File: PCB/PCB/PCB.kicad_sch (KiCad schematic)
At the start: 28 parts, among them J2 USB_B_Micro, Q1 BC817, Q2 BC817, Q3 BSS84, U1 ESP32-S3-WROOM-1, U2 CP2102N-Axx-xQFN28, U3 NCP1117-3.3_SOT223, U4 UDA1334ATS, U5 PAM8403D

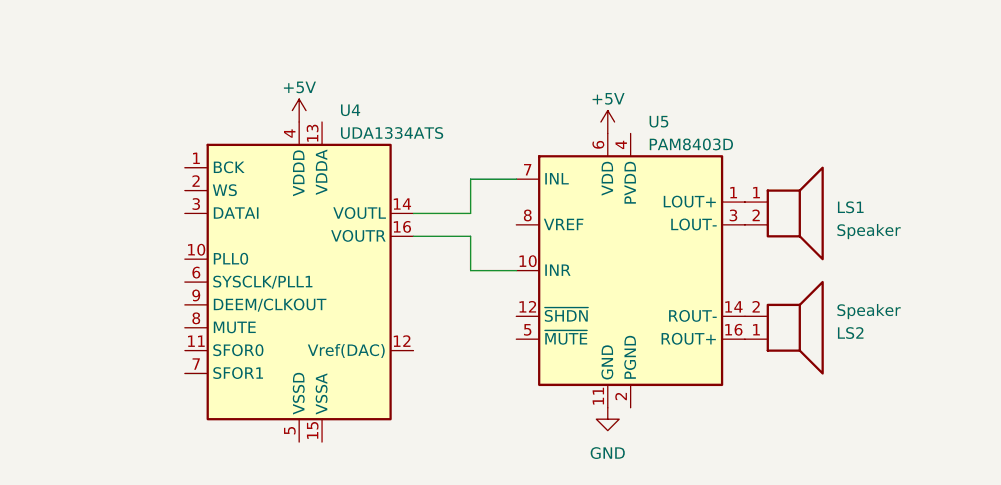
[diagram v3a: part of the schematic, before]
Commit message: added Audio Processing
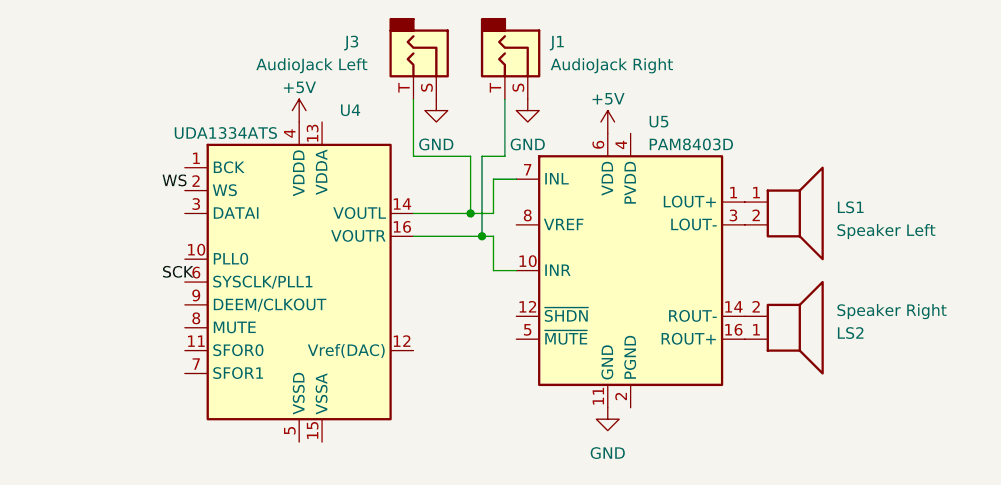
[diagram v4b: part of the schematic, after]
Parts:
- added J1: AudioJack Right, Connector_Audio:Jack_XLR_Neutrik_NC3FAAH1-0_Horizontal, symbol Connector_Audio:AudioJack2
- added J3: AudioJack Left, symbol Connector_Audio:AudioJack2
- LS1: value Speaker -> Speaker Left
- LS2: value Speaker -> Speaker Right
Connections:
- net GND: now also J1.S, J3.S
- net at U4.16 (VOUTR), U5.10 (INR): now also J1.T
- net at U4.14 (VOUTL), U5.7 (INL): now also J3.T
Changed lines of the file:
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@@
   (junction (at 41.91 93.98) (diameter 0) (color 0 0 0 0)
   )
+  (junction (at 314.96 36.83) (diameter 0) (color 0 0 0 0)
+  )
   (junction (at 50.8 81.28) (diameter 0) (color 0 0 0 0)
   )
@@
   )
   (junction (at 24.13 104.14) (diameter 0) (color 0 0 0 0)
+  )
+  (junction (at 313.69 34.29) (diameter 0) (color 0 0 0 0)
   )
   (junction (at 71.12 71.12) (diameter 0) (color 0 0 0 0)
@@
     (stroke (width 0) (type default))
   )
+  (wire (pts (xy 313.69 27.94) (xy 313.69 34.29))
+    (stroke (width 0) (type default))
+  )
+  (wire (pts (xy 314.96 36.83) (xy 316.23 36.83))
+    (stroke (width 0) (type default))
+  )
+  (wire (pts (xy 313.69 34.29) (xy 316.23 34.29))
+    (stroke (width 0) (type default))
+  )
   (wire (pts (xy 57.15 76.2) (xy 58.42 76.2))
     (stroke (width 0) (type default))
@@
     (stroke (width 0) (type default))
   )
-  (wire (pts (xy 313.69 34.29) (xy 313.69 30.48))
+  (wire (pts (xy 316.23 34.29) (xy 316.23 30.48))
     (stroke (width 0) (type default))
   )
@@
     (stroke (width 0) (type default))
   )
-  (wire (pts (xy 307.34 36.83) (xy 313.69 36.83))
+  (wire (pts (xy 307.34 36.83) (xy 314.96 36.83))
     (stroke (width 0) (type default))
   )
@@
     (stroke (width 0) (type default))
   )
-  (wire (pts (xy 313.69 30.48) (xy 318.77 30.48))
+  (wire (pts (xy 316.23 30.48) (xy 318.77 30.48))
     (stroke (width 0) (type default))
   )
@@
     (stroke (width 0) (type default))
   )
+  (wire (pts (xy 307.34 21.59) (xy 307.34 27.94))
+    (stroke (width 0) (type default))
+  )
   (wire (pts (xy 41.91 93.98) (xy 41.91 104.14))
     (stroke (width 0) (type default))
@@
     (stroke (width 0) (type default))
   )
-  (wire (pts (xy 313.69 36.83) (xy 313.69 40.64))
+  (wire (pts (xy 316.23 36.83) (xy 316.23 40.64))
     (stroke (width 0) (type default))
   )
@@
     (stroke (width 0) (type default))
   )
+  (wire (pts (xy 317.5 27.94) (xy 314.96 27.94))
+    (stroke (width 0) (type default))
+  )
   (wire (pts (xy 46.99 88.9) (xy 46.99 109.22))
     (stroke (width 0) (type default))
@@
     (stroke (width 0) (type default))
   )
+  (wire (pts (xy 314.96 27.94) (xy 314.96 36.83))
+    (stroke (width 0) (type default))
+  )
   (wire (pts (xy 116.84 60.96) (xy 144.78 60.96))
     (stroke (width 0) (type default))
@@
     (stroke (width 0) (type default))
   )
-  (wire (pts (xy 313.69 40.64) (xy 318.77 40.64))
+  (wire (pts (xy 316.23 40.64) (xy 318.77 40.64))
     (stroke (width 0) (type default))
   )
@@
     (stroke (width 0) (type default))
   )
+  (wire (pts (xy 307.34 27.94) (xy 313.69 27.94))
+    (stroke (width 0) (type default))
+  )
   (wire (pts (xy 111.76 78.74) (xy 111.76 46.99))
     (stroke (width 0) (type default))
@@
   )
   (wire (pts (xy 86.36 97.79) (xy 86.36 88.9))
+    (stroke (width 0) (type default))
+  )
+  (wire (pts (xy 317.5 21.59) (xy 317.5 27.94))
     (stroke (width 0) (type default))
   )
@@
     (effects (font (size 1.27 1.27)) (justify left bottom))
   )
+  (label "WS" (at 279.4 31.75 0) (fields_autoplaced)
+    (effects (font (size 1.27 1.27)) (justify left bottom))
+  )
   (label "txd" (at 83.82 76.2 0) (fields_autoplaced)
     (effects (font (size 1.27 1.27)) (justify left bottom))
@@
   )
   (label "EN" (at 113.03 83.82 0) (fields_autoplaced)
+    (effects (font (size 1.27 1.27)) (justify left bottom))
+  )
+  (label "SCK" (at 279.4 41.91 0) (fields_autoplaced)
     (effects (font (size 1.27 1.27)) (justify left bottom))
   )
@@
     )
   )
+  (symbol (lib_id "power:GND") (at 320.04 21.59 0) (unit 1)
+    (in_bom yes) (on_board yes) (dnp no) (fields_autoplaced)
+    (property "Reference" "#PWR021" (at 320.04 27.94 0)
+      (effects (font (size 1.27 1.27)) hide)
+    )
+    (property "Value" "GND" (at 320.04 26.67 0)
+      (effects (font (size 1.27 1.27)))
+    )
+    (property "Footprint" "" (at 320.04 21.59 0)
+      (effects (font (size 1.27 1.27)) hide)
+    )
+    (property "Datasheet" "" (at 320.04 21.59 0)
+      (effects (font (size 1.27 1.27)) hide)
+    )
+    (pin "1")
+    (instances
+      (project "PCB"
+        (path "/8a45fe01-405d-4f4d-910d-01ae941f9b06"
+          (reference "#PWR021") (unit 1)
+        )
+      )
+    )
+  )
   (symbol (lib_id "power:GND") (at 59.69 36.83 0) (unit 1)
     (in_bom yes) (on_board yes) (dnp no) (fields_autoplaced)
@@
       (effects (font (size 1.27 1.27)) (justify left))
     )
-    (property "Value" "Speaker" (at 354.33 36.195 0)
+    (property "Value" "Speaker Left" (at 354.33 36.195 0)
       (effects (font (size 1.27 1.27)) (justify left))
     )
@@
       (effects (font (size 1.27 1.27)) (justify left))
     )
-    (property "Value" "Speaker" (at 354.33 45.085 0)
+    (property "Value" "Speaker Right" (at 354.33 45.085 0)
       (effects (font (size 1.27 1.27)) (justify left))
     )
@@
   )
   (symbol (lib_id "Audio:UDA1334ATS") (at 294.64 41.91 0) (unit 1)
-    (in_bom yes) (on_board yes) (dnp no) (fields_autoplaced)
+    (in_bom yes) (on_board yes) (dnp no)
     (property "Reference" "U4" (at 299.1359 22.86 0)
       (effects (font (size 1.27 1.27)) (justify left))
     )
-    (property "Value" "UDA1334ATS" (at 299.1359 25.4 0)
+    (property "Value" "UDA1334ATS" (at 280.67 25.4 0)
       (effects (font (size 1.27 1.27)) (justify left))
     )
@@
         (path "/8a45fe01-405d-4f4d-910d-01ae941f9b06"
           (reference "R7") (unit 1)
+        )
+      )
+    )
+  )
+  (symbol (lib_id "power:GND") (at 309.88 21.59 0) (unit 1)
+    (in_bom yes) (on_board yes) (dnp no)
+    (property "Reference" "#PWR022" (at 309.88 27.94 0)
+      (effects (font (size 1.27 1.27)) hide)
+    )
+    (property "Value" "GND" (at 309.88 26.67 0)
+      (effects (font (size 1.27 1.27)))
+    )
+    (property "Footprint" "" (at 309.88 21.59 0)
+      (effects (font (size 1.27 1.27)) hide)
+    )
+    (property "Datasheet" "" (at 309.88 21.59 0)
+      (effects (font (size 1.27 1.27)) hide)
+    )
+    (pin "1")
+    (instances
+      (project "PCB"
+        (path "/8a45fe01-405d-4f4d-910d-01ae941f9b06"
+          (reference "#PWR022") (unit 1)
         )
       )
@@
     )
   )
+  (symbol (lib_id "Connector_Audio:AudioJack2") (at 307.34 16.51 270) (unit 1)
+    (in_bom yes) (on_board yes) (dnp no)
+    (property "Reference" "J3" (at 299.72 15.24 90)
+      (effects (font (size 1.27 1.27)) (justify left))
+    )
+    (property "Value" "AudioJack Left" (at 302.26 17.78 90)
+      (effects (font (size 1.27 1.27)) (justify right))
+    )
+    (property "Footprint" "" (at 307.34 16.51 0)
+      (effects (font (size 1.27 1.27)) hide)
+    )
+    (property "Datasheet" "~" (at 307.34 16.51 0)
+      (effects (font (size 1.27 1.27)) hide)
+    )
+    (pin "S")
+    (pin "T")
+    (instances
+      (project "PCB"
+        (path "/8a45fe01-405d-4f4d-910d-01ae941f9b06"
+          (reference "J3") (unit 1)
+        )
+      )
+    )
+  )
   (symbol (lib_id "Device:R") (at 109.22 107.95 90) (unit 1)
     (in_bom yes) (on_board yes) (dnp no)
@@
         )
       )
+    )
+  )
+  (symbol (lib_id "Connector_Audio:AudioJack2") (at 317.5 16.51 270) (unit 1)
+    (in_bom yes) (on_board yes) (dnp no) (fields_autoplaced)
+    (property "Reference" "J1" (at 322.58 15.24 90)
+      (effects (font (size 1.27 1.27)) (justify left))
+    )
+    (property "Value" "AudioJack Right" (at 322.58 17.78 90)
+      (effects (font (size 1.27 1.27)) (justify left))
+    )
+    (property "Footprint" "Connector_Audio:Jack_XLR_Neutrik_NC3FAAH1-0_Horizontal" (at 317.5 16.51 0)
+      (effects (font (size 1.27 1.27)) hide)
+    )
+    (property "Datasheet" "~" (at 317.5 16.51 0)
+      (effects (font (size 1.27 1.27)) hide)
+    )
+    (pin "S")
+    (pin "T")
+    (instances
+      (project "PCB"
+        (path "/8a45fe01-405d-4f4d-910d-01ae941f9b06"
+          (reference "J1") (unit 1)
+        )
+      )

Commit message: edit Vorlesung
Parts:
- added C10, C13, C15, C7: 47µF, symbol Device:C
- added C11, C12: 10nF, symbol Device:C
- added C14, C6, C8: 100nF, symbol Device:C
- added C16, C9: 10µF, symbol Device:C
- added D5: LED, symbol Device:LED
- added D6: PWR_LED, symbol Device:LED
- added J4: 6PIN DISPLAY CONNECTOR, symbol Connector:Conn_01x06_Pin
- added R10, R12: 220, symbol Device:R
- added R11, R13: 100, symbol Device:R
- added R14: 470, symbol Device:R
- added R15: 2K, symbol Device:R
- added R16: 10K, symbol Device:R
- added R9: 1, symbol Device:R
- added U6: MCP73831-3-OT, Package_TO_SOT_SMD:SOT-23-5, symbol Battery_Management:MCP73831-3-OT
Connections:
- net +3.3V: now also C9.2, J4.2 (Pin_2), R16.2, R9.1
- net +BATT: now also U6.3 (V_{BAT})
- net GND: now also U4.10 (PLL0), U4.11 (SFOR0), U4.13 (VDDA), U4.15 (VSSA), U4.4 (VDDD), U4.5 (VSSD), U4.6 (SYSCLK/PLL1), U4.7 (SFOR1), U4.9 (DEEM/CLKOUT), U5.15 (PGND), U5.2 (PGND), C11.2, C12.1, C14.2, C15.2, C16.2, C6.1, C7.1, C8.1, D6.1 (K), J4.1 (Pin_1), R10.2, R12.1, R15.2, U6.2 (V_{SS})
- net VBUS: now also C16.1, R14.1, U6.4 (V_{DD})
- net at U1.12 (GPIO8/TOUCH8/ADC1_CH7/SUBSPICS1): now also J4.3 (Pin_3)
- net at U1.15 (GPIO3/TOUCH3/ADC1_CH2): now also U4.3 (DATAI)
- net at U1.38 (GPIO2/TOUCH2/ADC1_CH1): now also U4.2 (WS)
- net at U1.39 (GPIO1/TOUCH1/ADC1_CH0): now also U4.1 (BCK)
- net at U1.4 (GPIO4/TOUCH4/ADC1_CH3): now also U4.8 (MUTE)
- net at U1.5 (GPIO5/TOUCH5/ADC1_CH4): now also J4.6 (Pin_6)
- net at U1.6 (GPIO6/TOUCH6/ADC1_CH5): now also J4.5 (Pin_5)
- net at U1.7 (GPIO7/TOUCH7/ADC1_CH6): now also J4.4 (Pin_4)
- net at J1.T, U5.10 (INR): now also C12.2, R13.2; no longer U4.16 (VOUTR)
- net at U5.13 (PVDD), U5.4 (PVDD): now also U5.6 (VDD), C9.1
- net at J3.T, U5.7 (INL): now also C11.1, R11.2; no longer U4.14 (VOUTL)
- net at U5.8 (VREF): now also C8.2
- net at U4.12 (Vref(DAC)): now also C14.1, C15.1
- removed net +5V: U4.4 (VDDD), U5.6 (VDD)
- new net: R15.1, U6.5 (PROG)
- new net: C6.2, C7.2, R9.2
- new net: D6.2 (A), R16.1
- new net: C13.1, U4.16 (VOUTR)
- new net: C13.2, R12.2, R13.1
- new net: C10.1, U4.14 (VOUTL)
- new net: C10.2, R10.1, R11.1
- new net: D5.2 (A), R14.2
- new net: D5.1 (K), U6.1 (STAT)
- no-connect marks 13 -> 28
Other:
- moved on the sheet: U4
